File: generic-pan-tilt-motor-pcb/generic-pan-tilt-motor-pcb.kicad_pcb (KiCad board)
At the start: 2 copper layers, 0 parts

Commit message: motor basic layout
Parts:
- added C1: 1µF 16V, Capacitor_SMD:C_0603_1608Metric, F.Cu at (-92.9, 25.9)
- added C10: 1uF 50V, Capacitor_SMD:C_0603_1608Metric, F.Cu at (110.0, 111.2)
- added C11: 0.1uF 16V, Capacitor_SMD:C_0603_1608Metric, F.Cu at (-31.9, 10.6)
- added C12: 22nF 50V, Capacitor_SMD:C_0603_1608Metric, F.Cu at (108.2, 109.3)
- added C13: 2.2uF 16V, Capacitor_SMD:C_0603_1608Metric, F.Cu at (117.7, 103.9)
- added C14: 1nF 100V, Capacitor_SMD:C_0603_1608Metric, F.Cu at (-27.9, 8.06)
- added C15: 1nF 100V, Capacitor_SMD:C_0603_1608Metric, F.Cu at (-27.9, 10.6)
- added C16: 1nF 100V, Capacitor_SMD:C_0603_1608Metric, F.Cu at (-27.9, 13.1)
- added C17: 1nF 100V, Capacitor_SMD:C_0603_1608Metric, F.Cu at (-27.9, 15.6)
- added C18: 0.1µF 16V, Capacitor_SMD:C_0402_1005Metric, F.Cu at (-37.6, 23.8)
- added C19: 15pF 50V, Capacitor_SMD:C_0603_1608Metric, F.Cu at (-47.1, 35.3)
- added C2: 1µF 16V, Capacitor_SMD:C_0603_1608Metric, F.Cu at (-92.9, 28.4)
- added C20: 15pF 50V, Capacitor_SMD:C_0603_1608Metric, F.Cu at (-47.1, 37.8)
- added C21: 15pF 50V, Capacitor_SMD:C_0603_1608Metric, F.Cu at (-47.1, 40.3)
- added C22: 0.1µF 16V, Capacitor_SMD:C_0402_1005Metric, F.Cu at (-43.6, 35.0)
- added C3: 1µF 16V, Capacitor_SMD:C_0603_1608Metric, F.Cu at (-92.9, 30.9)
- added C4: 150uF 50V, Capacitor_SMD:CP_Elec_10x10, F.Cu at (106.0, 104.9)
- added C5: 0.1uF 50V, Capacitor_SMD:C_0603_1608Metric, F.Cu at (-35.9, 8.06)
- added C6: 1uF 50V, Capacitor_SMD:C_0603_1608Metric, F.Cu at (-35.9, 10.6)
- added C7: 150uF 50V, Capacitor_SMD:CP_Elec_10x10, F.Cu at (128.4, 105.3)
- added C8: 0.1uF 50V, Capacitor_SMD:C_0603_1608Metric, F.Cu at (-35.9, 13.1)
- added C9: 1uF 50V, Capacitor_SMD:C_0603_1608Metric, F.Cu at (-35.9, 15.6)
- added D1: TPSMB30A, Diode_SMD:D_SMB, F.Cu at (-71.7, 34.3)
- added D2: SML-E12M8WT86, LED_SMD:LED_0603_1608Metric, F.Cu at (-56.9, 21.5)
- added D3: SML-E12V8WT86, LED_SMD:LED_0603_1608Metric, F.Cu at (-56.9, 24.1)
- added D4: SML-E12D8WT86, LED_SMD:LED_0603_1608Metric, F.Cu at (-56.9, 26.6)
- added D5: MSS1P6-M3/89A, Diode_SMD:D_MicroSMP_AK, F.Cu at (-32.3, 1.55)
- added FID1: Fiducial, Fiducial:Fiducial_0.5mm_Mask1mm, F.Cu at (-60.2, 21.4)
- added FID2: Fiducial, Fiducial:Fiducial_0.5mm_Mask1mm, F.Cu at (-60.2, 24.0)
- added FID3: Fiducial, Fiducial:Fiducial_0.5mm_Mask1mm, F.Cu at (-60.2, 26.6)
- added FID4: Fiducial, Fiducial:Fiducial_0.5mm_Mask1mm, F.Cu at (-60.2, 29.1)
- added H1: MountingHole, MountingHole:MountingHole_3.2mm_M3, F.Cu at (98.0, 93.0)
- added H2: MountingHole, MountingHole:MountingHole_3.2mm_M3, F.Cu at (165.0, 93.0)
- added H3: MountingHole, MountingHole:MountingHole_3.2mm_M3, F.Cu at (98.0, 115.0)
- added H4: MountingHole, MountingHole:MountingHole_3.2mm_M3, F.Cu at (165.0, 115.0)
- added J1: B12B-PH-SM4-TBT, Connector_JST:JST_PH_B12B-PH-SM4-TB_1x12-1MP_P2.00mm_Vertical, F.Cu at (117.0, 94.2)
- added J2: S4B-PH-SM4-TB, Connector_JST:JST_PH_B4B-PH-SM4-TB_1x04-1MP_P2.00mm_Vertical, F.Cu at (139.0, 94.3)
- added J3: S4B-PH-SM4-TB, Connector_JST:JST_PH_B4B-PH-SM4-TB_1x04-1MP_P2.00mm_Vertical, F.Cu at (153.1, 94.2)
- added J4: 1945096, generic-pan-tilt-motor-pcb:PhoenixContact_PST_1.0_2-3.5_1x02_P3.5mm_Vertical, F.Cu at (154.7, 115.0)
- added J5: 1945119, generic-pan-tilt-motor-pcb:PhoenixContact_PST_1.0_4-3.5_1x04_P3.5mm_Vertical, F.Cu at (106.5, 115.2)
- added J6: 1945151, generic-pan-tilt-motor-pcb:PhoenixContact_PST_1.0_8-3.5_1x08_P3.5mm_Vertical, F.Cu at (123.0, 115.1)
- added JP1: SolderJumper_3_Bridged12, Jumper:SolderJumper-3_P1.3mm_Bridged12_RoundedPad1.0x1.5mm_NumberLabels, F.Cu at (112.8, 76.2)
- added JP2: SolderJumper_3_Bridged12, Jumper:SolderJumper-3_P1.3mm_Bridged12_RoundedPad1.0x1.5mm_NumberLabels, F.Cu at (119.5, 73.0)
- added JP3: SolderJumper_3_Bridged12, Jumper:SolderJumper-3_P1.3mm_Bridged12_RoundedPad1.0x1.5mm_NumberLabels, F.Cu at (113.0, 73.0)
- added Q1: DMN6075S, Package_TO_SOT_SMD:SOT-23, F.Cu at (-27.7, 2.52)
- added R1: 55Ω, Resistor_SMD:R_0402_1005Metric, F.Cu at (-89.5, 25.7)
- added R10: 12kΩ, Resistor_SMD:R_0402_1005Metric, F.Cu at (120.6, 103.4)
- added R11: 10kΩ, Resistor_SMD:R_0402_1005Metric, F.Cu at (-37.6, 19.8)
- added R12: 10kΩ, Resistor_SMD:R_0402_1005Metric, F.Cu at (-37.6, 21.8)
- added R13: 4.7kΩ, Resistor_SMD:R_0402_1005Metric, F.Cu at (-50.5, 35.0)
- added R14: 4.7kΩ, Resistor_SMD:R_0402_1005Metric, F.Cu at (-50.5, 37.0)
- added R15: 4.7kΩ, Resistor_SMD:R_0402_1005Metric, F.Cu at (-50.5, 39.0)
- added R16: 1kΩ, Resistor_SMD:R_0402_1005Metric, F.Cu at (-50.5, 41.0)
- added R17: 1kΩ, Resistor_SMD:R_0402_1005Metric, F.Cu at (-50.5, 43.0)
- added R18: 1kΩ, Resistor_SMD:R_0402_1005Metric, F.Cu at (-50.5, 45.0)
- added R2: 55Ω, Resistor_SMD:R_0402_1005Metric, F.Cu at (-89.5, 27.7)
- added R3: 1.2kΩ 1W, Resistor_SMD:R_2512_6332Metric, F.Cu at (-71.5, 29.1)
- added R4: 4.7kΩ, Resistor_SMD:R_0402_1005Metric, F.Cu at (-36.4, -6.13)
- added R5: 15.8kΩ, Resistor_SMD:R_0402_1005Metric, F.Cu at (-36.4, -4.14)
- added R6: 4.7kΩ, Resistor_SMD:R_0402_1005Metric, F.Cu at (-36.4, -2.15)
- added R7: 4.7kΩ, Resistor_SMD:R_0402_1005Metric, F.Cu at (-36.4, -0.16)
- added R8: 4.7kΩ, Resistor_SMD:R_0402_1005Metric, F.Cu at (-36.4, 1.83)
- added R9: 4.7kΩ, Resistor_SMD:R_0402_1005Metric, F.Cu at (-36.4, 3.82)
- added SYM1: Logo_Open_Hardware_Small, Symbol:OSHW-Logo2_7.3x6mm_SilkScreen, F.Cu at (175.8, 81.8)
- added TP1: TestPoint, TestPoint:TestPoint_Pad_1.0x1.0mm, F.Cu at (-60.1, 5.65)
- added TP2: TestPoint, TestPoint:TestPoint_Pad_1.0x1.0mm, F.Cu at (-60.1, 8.70)
- added TP3: TestPoint, TestPoint:TestPoint_Pad_1.0x1.0mm, F.Cu at (-60.1, 11.8)
- added TP4: TestPoint, TestPoint:TestPoint_Pad_1.0x1.0mm, F.Cu at (-60.1, 14.8)
- added TP5: TestPoint, TestPoint:TestPoint_Pad_1.0x1.0mm, F.Cu at (-57.0, 5.65)
- added TP6: TestPoint, TestPoint:TestPoint_Pad_1.0x1.0mm, F.Cu at (-57.0, 8.70)
- added TP7: TestPoint, TestPoint:TestPoint_Pad_1.0x1.0mm, F.Cu at (-57.0, 11.8)
- added U1: TMC5240ATJ+, Package_DFN_QFN:TQFN-32-1EP_5x5mm_P0.5mm_EP3.1x3.1mm_ThermalVias, F.Cu at (116.5, 108.2)
- added U2: MCP23S08-xSO, Package_SO:SOIC-18W_7.5x11.6mm_P1.27mm, F.Cu at (-45.5, 25.5)
- added U3: 74LVC3G17, Package_SO:VSSOP-8_2.3x2mm_P0.5mm, F.Cu at (-45.9, 43.4)
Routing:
- net +24V: track 0.00 -> 38.5 mm, vias 0 -> 4
- net /SPI_CS_CNTLR: track 0.00 -> 25.8 mm, vias 0 -> 2
- net /ENC_N_FILTERED: track 0.00 -> 22.8 mm, vias 0 -> 1
- net /generic-pan-tilt-motor-pcb_driver/OV: track 0.00 -> 22.6 mm, vias 0 -> 1
- net /ENC_B_FILTERED: track 0.00 -> 22.1 mm, vias 0 -> 1
- net /MOT_DIAG0: track 0.00 -> 22.0 mm, vias 0 -> 1
- net /MOT_DIAG1: track 0.00 -> 21.6 mm, vias 0 -> 1
- net /~{MOT_DRV_ENN}: track 0.00 -> 21.1 mm, vias 0 -> 1
- net /SPI_POCI: track 0.00 -> 20.9 mm, vias 0 -> 2
- net /SPI_PICO: track 0.00 -> 20.8 mm, vias 0 -> 2
- net /SPI_SCK: track 0.00 -> 20.6 mm, vias 0 -> 2
- net /ENC_A_FILTERED: track 0.00 -> 20.5 mm, vias 0 -> 1
- net +3V3: track 0.00 -> 16.8 mm, vias 0 -> 2
- net /OUT2B: track 0.00 -> 14.4 mm
- net /~{MOT_SLEEPN}: track 0.00 -> 12.9 mm, vias 0 -> 1
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- added copper zone on B.Cu, net GND
- added copper zone on F.Cu, net GND
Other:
- board outline added: 73 x 28 mm

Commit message: motor pcb layout up to enc filter
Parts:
- C18, C22: footprint Capacitor_SMD:C_0402_1005Metric -> Capacitor_SMD:C_0603_1608Metric
- moved R3 256.1 mm to (166.0, 125.0)
- moved D4 238.0 mm to (160.3, 124.0)
- moved D5 235.4 mm to (165.5, 129.2)
- moved Q1 224.1 mm to (158.3, 127.5)
- moved D1 220.9 mm to (138.0, 103.9), turned to -90 degrees
- moved C22 209.3 mm to (145.0, 125.7)
- moved R13 209.3 mm to (138.1, 125.7)
- moved R14 209.3 mm to (138.1, 127.7)
- moved R15 209.3 mm to (138.1, 129.7)
- moved R18 205.4 mm to (144.2, 110.2), turned to 180 degrees
- moved R17 205.2 mm to (144.2, 107.8), turned to 180 degrees
- moved R16 205.0 mm to (144.2, 105.2), turned to 180 degrees
- moved C21 202.4 mm to (142.4, 111.2), turned to -90 degrees
- moved C20 202.2 mm to (142.4, 108.2), turned to -90 degrees
- moved C19 202.0 mm to (142.4, 105.2), turned to -90 degrees
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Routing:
- net +3V3: track 16.8 -> 81.2 mm
- net /REF_L: track 2.85 -> 52.2 mm, vias 1 -> 4
- net /REF_R: track 3.39 -> 47.3 mm, vias 1 -> 2
- net /ENC_N+: track 0.00 -> 31.9 mm, vias 0 -> 1
- net /ENC_B+: track 0.00 -> 29.9 mm, vias 0 -> 1
- net /ENC_A+: track 0.00 -> 29.4 mm, vias 0 -> 1
- net /ENC_N_FILTERED: track 22.8 -> 50.0 mm, vias 1 -> 2
- net /ENC_N-: track 0.00 -> 26.8 mm, vias 0 -> 1
- net /ENC_A_FILTERED: track 20.5 -> 45.7 mm, vias 1 -> 2
- net /ENC_B_FILTERED: track 22.1 -> 44.6 mm, vias 1 -> 2
- net /ENC_B-: track 0.00 -> 22.4 mm, vias 0 -> 1
- net /generic-pan-tilt-motor-pcb_driver/OV: track 22.6 -> 1.53 mm
- net /ENC_A-: track 0.00 -> 19.5 mm, vias 0 -> 1
- net +24V: track 38.5 -> 57.5 mm, vias 4 -> 3
- net /~{MOT_DRV_ENN}: track 21.1 -> 4.05 mm
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
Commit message: motor all placed
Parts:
- added FID5: Fiducial, Fiducial:Fiducial_0.5mm_Mask1mm, B.Cu at (96.8, 97.8)
- added FID6: Fiducial, Fiducial:Fiducial_0.5mm_Mask1mm, B.Cu at (162.0, 111.8)
- JP1, JP2, JP3, SYM1, TP1, TP2, TP3, TP4, TP5, TP6, TP7: moved to B.Cu
- moved C2 253.6 mm to (150.5, 99.5)
- moved TP2 245.5 mm to (165.5, 105.5), turned to 180 degrees
- moved C3 243.2 mm to (137.2, 109.4)
- moved TP4 242.4 mm to (165.5, 103.5), turned to 180 degrees
- moved TP1 242.2 mm to (161.5, 103.5), turned to 180 degrees
- moved C1 241.9 mm to (137.5, 99.5)
- moved TP3 241.7 mm to (163.5, 103.5), turned to 180 degrees
- moved FID4 234.2 mm to (158.8, 112.0)
- moved FID3 233.9 mm to (162.8, 97.0)
- moved TP5 231.3 mm to (152.2, 104.0), turned to 180 degrees
- moved R2 230.2 mm to (153.0, 101.2)
- moved TP6 229.2 mm to (152.2, 102.0), turned to 180 degrees
- moved D3 228.4 mm to (154.8, 100.8), turned to 90 degrees
- moved TP7 226.1 mm to (150.2, 102.0), turned to 180 degrees
- moved R4 222.3 mm to (154.5, 107.6)
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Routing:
- net GND: track 7.56 -> 127.1 mm, vias 104 -> 123
- net +3V3: track 81.2 -> 162.7 mm, vias 2 -> 4
- net /MOT_DIAG1: track 7.05 -> 85.5 mm, vias 1 -> 2
- net /~{MOT_DRV_ENN}: track 4.05 -> 82.2 mm, vias 1 -> 2
- net /MOT_DIAG0: track 5.65 -> 83.8 mm, vias 1 -> 2
- net /~{MOT_SLEEPN}: track 1.79 -> 79.4 mm, vias 1 -> 4
- net /SPI_PICO: track 24.0 -> 84.0 mm, vias 2 -> 4
- net /generic-pan-tilt-motor-pcb_driver/OV: track 1.53 -> 61.3 mm, vias 1 -> 2
- net /SPI_CS_GPIO: track 0.00 -> 59.6 mm, vias 0 -> 2
- net /SPI_POCI: track 22.6 -> 82.0 mm, vias 2 -> 4
- net /SPI_SCK: track 22.0 -> 80.6 mm, vias 2 -> 4
- net +24V: track 57.5 -> 98.7 mm, vias 3 -> 6
- net /ENC_N+: track 31.9 -> 5.22 mm, vias 1 -> 0
- net /ENC_B+: track 29.9 -> 3.67 mm, vias 1 -> 0
- net /ENC_A+: track 29.4 -> 5.47 mm, vias 1 -> 0
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
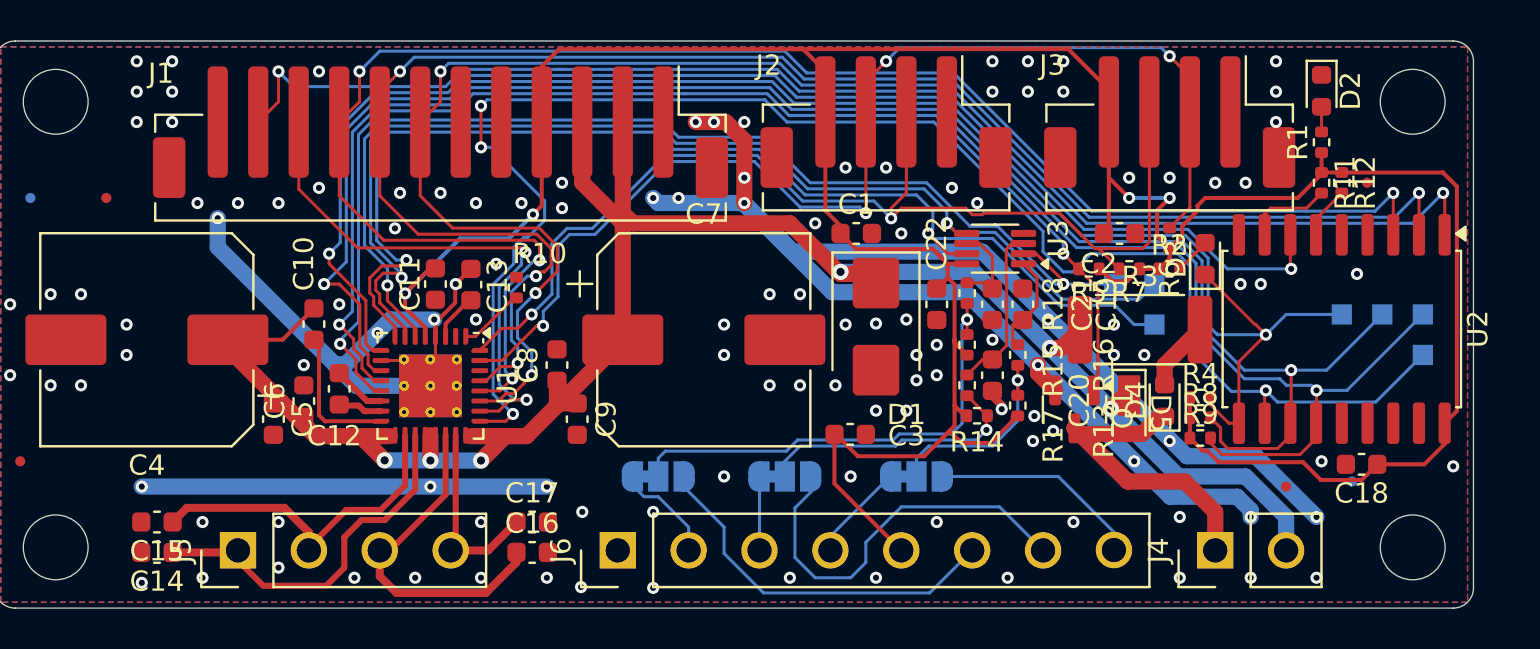
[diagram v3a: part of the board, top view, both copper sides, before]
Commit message: motor silkscreen done
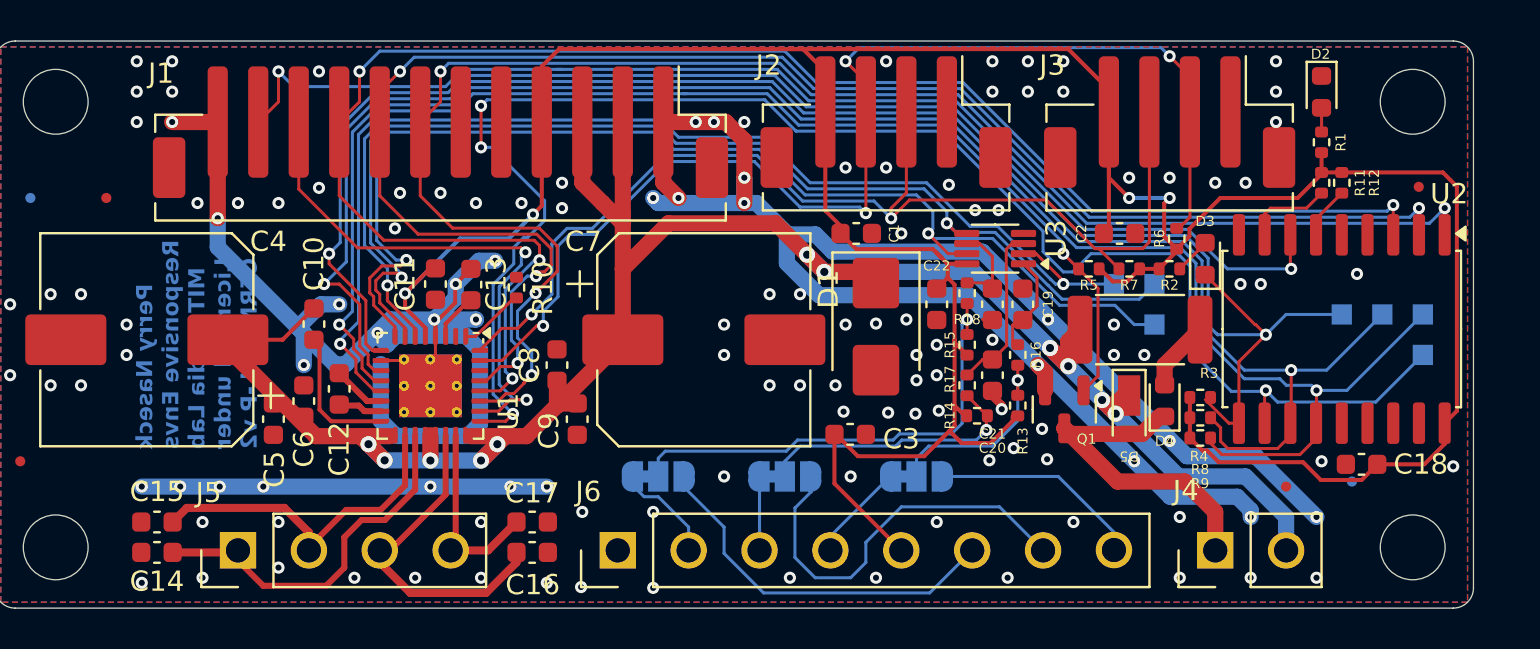
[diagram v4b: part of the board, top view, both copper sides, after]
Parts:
- moved SYM1 35.3 mm to (107.0, 94.5)
- moved FID3 2.56 mm to (165.3, 97.2)
- moved Q1 0.50 mm to (147.8, 108.2)
- moved R6 0.35 mm to (153.3, 99.8)
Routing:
- net GND: track 127.1 -> 162.6 mm, vias 123 -> 131
- net +24V: track 98.7 -> 106.8 mm, vias 6 -> 11
- net /REF_L: track 58.2 -> 60.1 mm
- net /SPI_POCI: track 82.0 -> 80.9 mm
- net /SPI_SCK: track 80.6 -> 79.6 mm
- net /OV_BRAKE_R-: track 15.5 -> 16.5 mm
- net /SPI_PICO: track 84.0 -> 83.2 mm
- net +3V3: track 162.7 -> 162.1 mm
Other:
- board text added: "Licensed under CERN-OHL-P v2"
- board text added: "Perry Naseck Responsive Envs MIT Media Lab"
- board text added: "Rev: ${KIBOT_GIT_DESCRIBE} ${KIBOT_GIT_DATE} ${KITBOT_RUN_DATE}"
- board text added: "https://github.com/mitmedialab/generic-pan-tilt-pcb/"

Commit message: motor resolve all drc
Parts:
- moved C2 0.43 mm to (150.1, 99.5)
- moved C8 0.40 mm to (123.0, 105.7)
- moved R6 0.36 mm to (153.3, 99.4)
- moved R5 0.35 mm to (149.0, 100.9)
- moved R2 0.35 mm to (153.0, 100.9)
- moved R7 0.35 mm to (151.0, 100.9)
- moved R13 0.10 mm to (145.6, 108.0)
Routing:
- net GND: track 162.6 -> 155.0 mm, vias 131 -> 132
- net +24V: track 106.8 -> 108.1 mm
- net /MOT_DIAG0: track 83.8 -> 84.7 mm

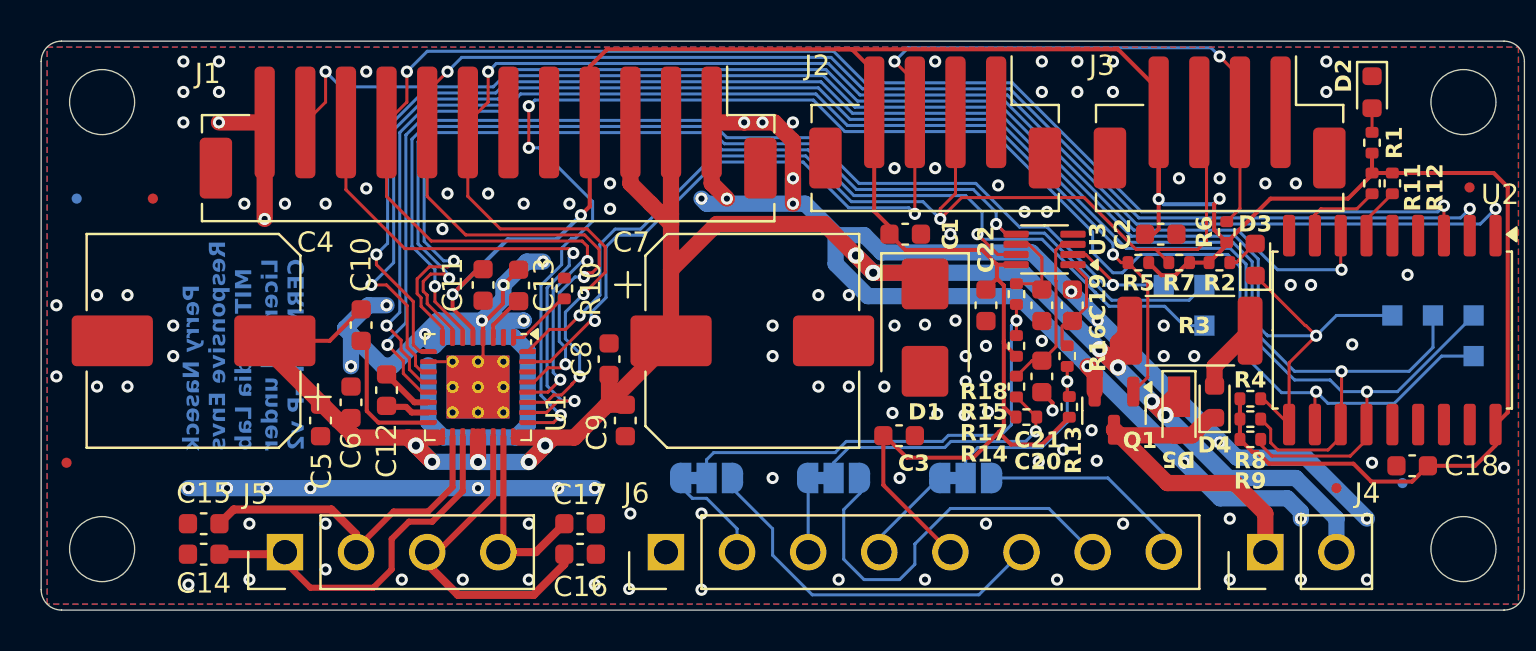
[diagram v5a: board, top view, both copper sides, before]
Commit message: add model def for 4 pin jst ph, add more motor gnd vias, align motor 12 pin connector
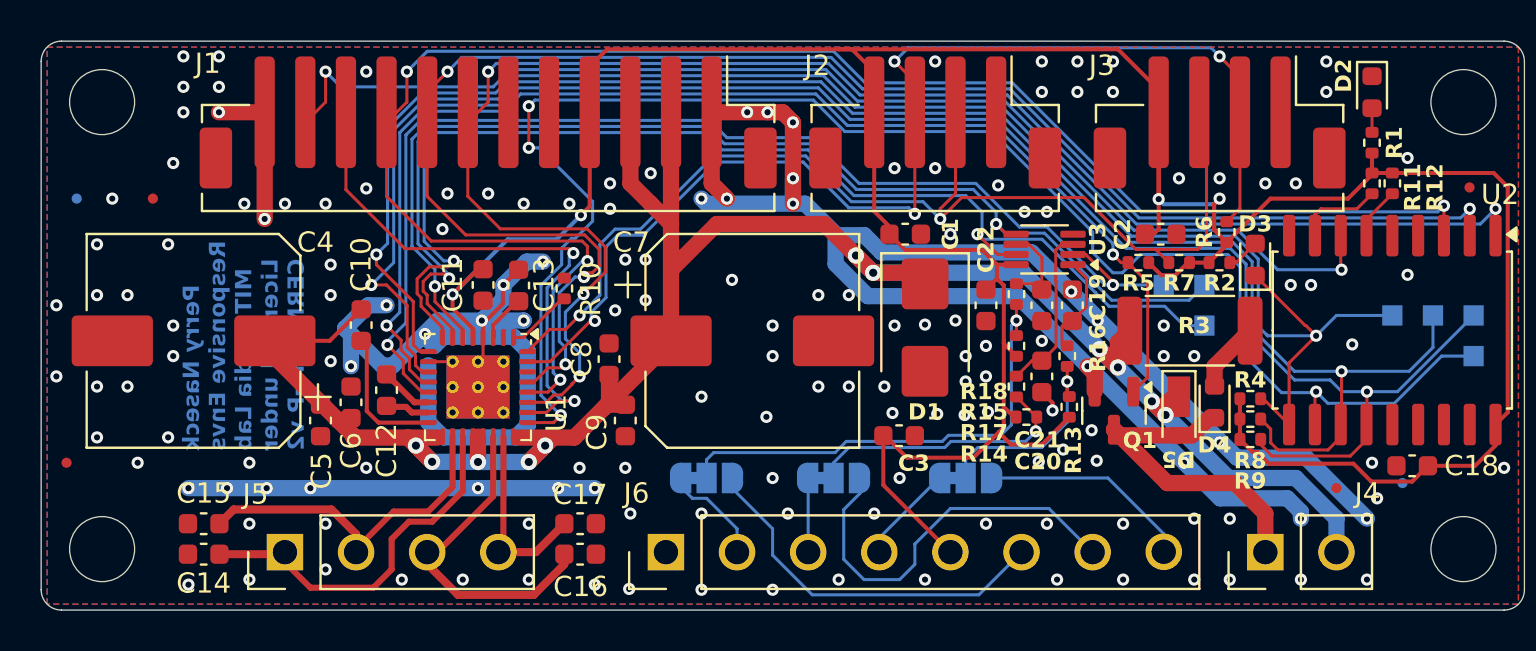
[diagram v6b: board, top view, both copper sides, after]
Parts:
- moved J1 0.50 mm to (117.0, 94.0)
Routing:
- net GND: track 155.0 -> 155.8 mm, vias 132 -> 163

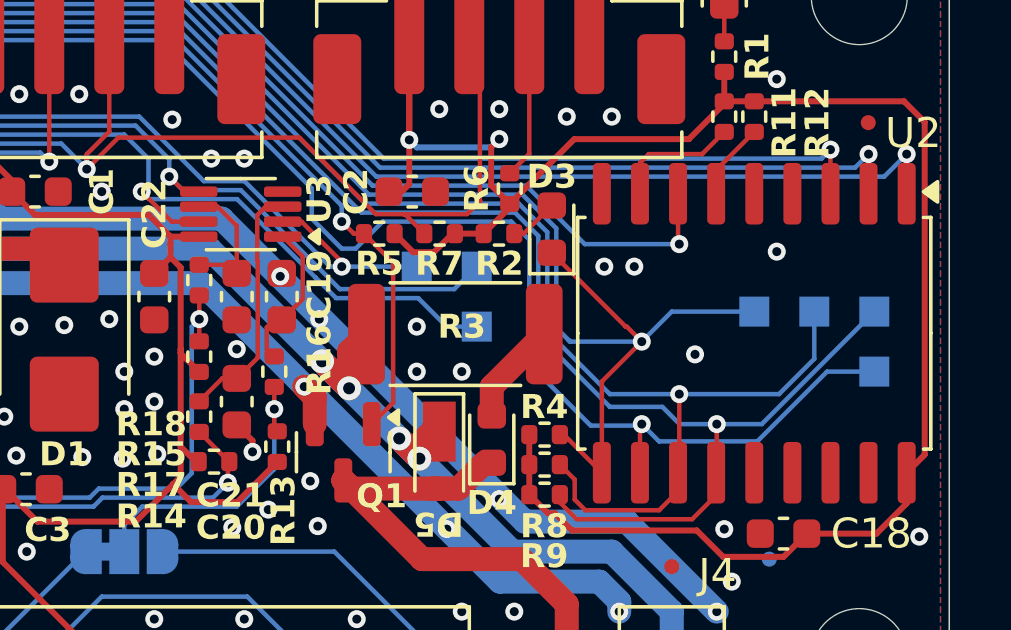
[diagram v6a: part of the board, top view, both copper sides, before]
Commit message: motor pcb vssop pad clearance increase to 0.19mm for pcbway soldermask
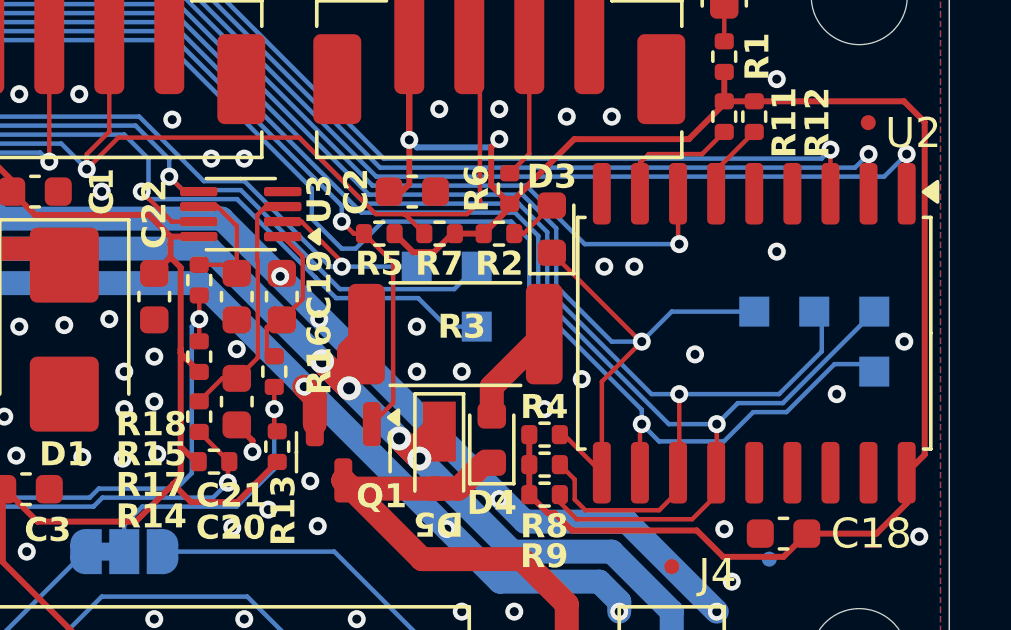
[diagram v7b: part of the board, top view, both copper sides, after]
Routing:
- net /~{MOT_DRV_ENN}: track 81.9 -> 81.0 mm
- net /~{MOT_SLEEPN}: track 79.4 -> 78.5 mm
- net /MOT_DIAG1: track 85.5 -> 84.7 mm
- net /MOT_DIAG0: track 84.7 -> 84.1 mm
- net GND: vias 163 -> 167
